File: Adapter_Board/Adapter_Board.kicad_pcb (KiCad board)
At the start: 2 copper layers, 10.7 x 10.8 mm, 2 parts, among them J1 Conn_02x04_Counter_Clockwise, J2 SOIC-8

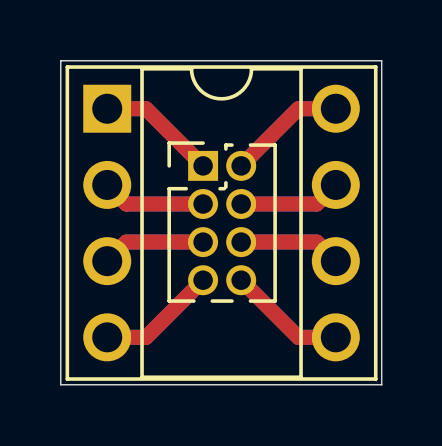
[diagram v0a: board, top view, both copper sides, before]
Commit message: Adjust the adapter board trace line width to 0.8 mm
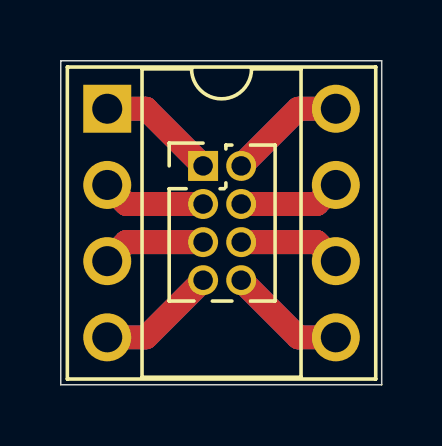
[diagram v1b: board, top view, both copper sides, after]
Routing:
- net Net-(J1-Pad2): track 10.4 -> 6.92 mm

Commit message: bump version to 2.0
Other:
- net class Default removed
